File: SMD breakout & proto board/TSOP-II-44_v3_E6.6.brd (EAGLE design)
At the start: 25.4 x 27.9 mm, 7 parts

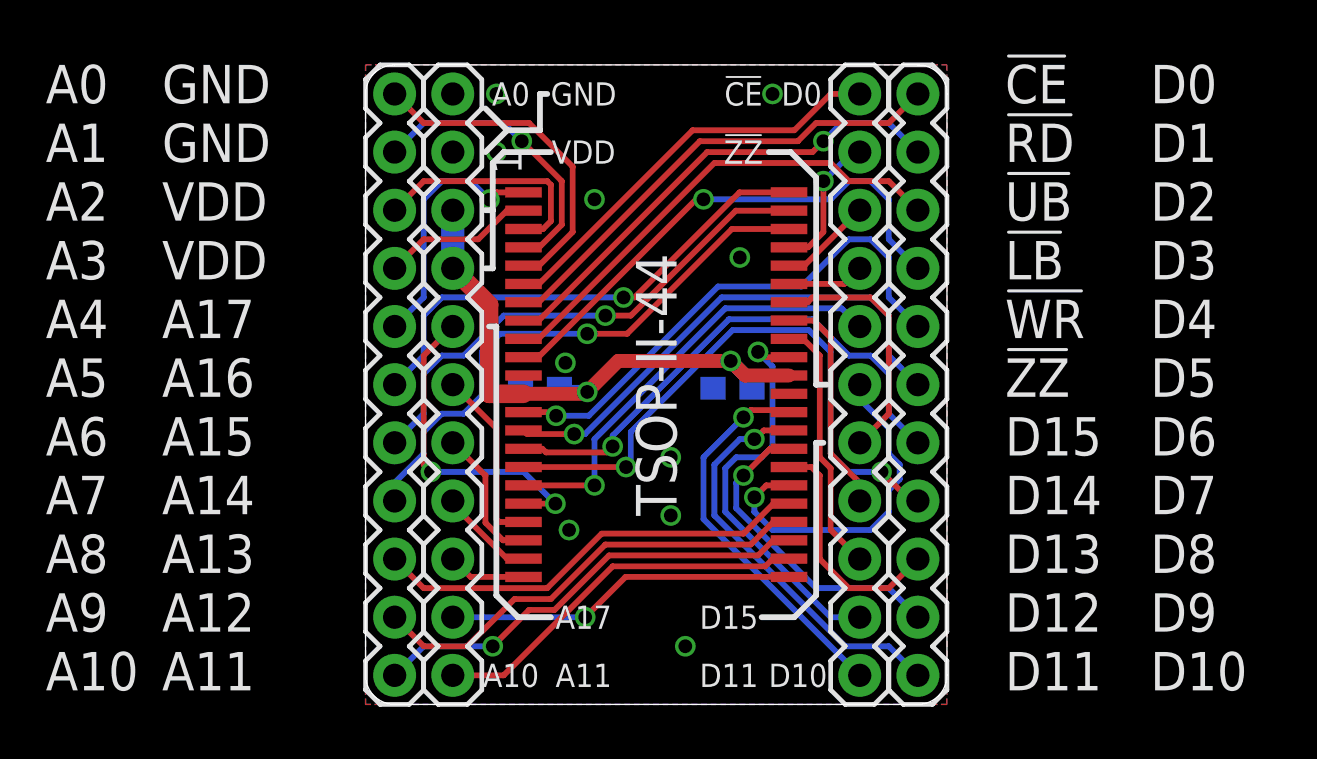
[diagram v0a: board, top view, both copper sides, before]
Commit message: swapped supply pins
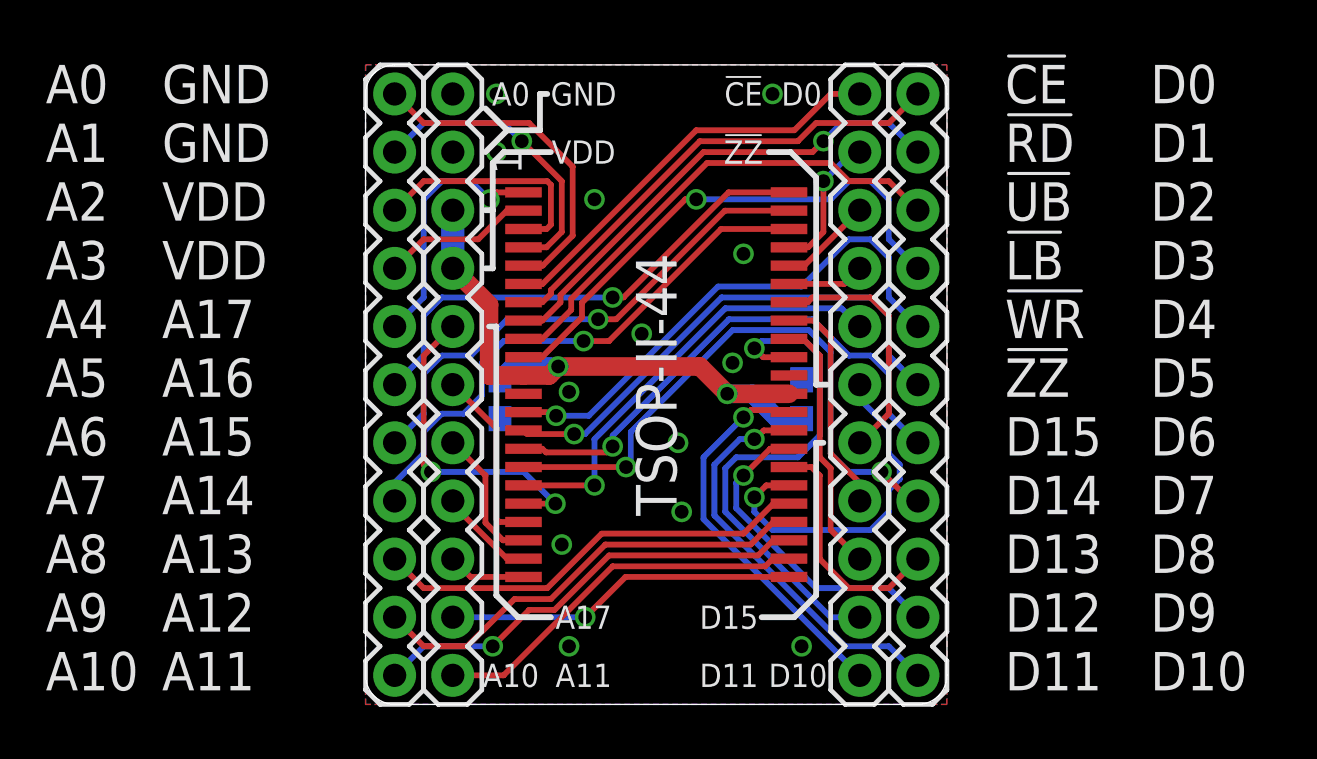
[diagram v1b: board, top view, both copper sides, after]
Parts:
- moved C2 3.05 mm to (19.1, 13.3), turned to 90 degrees
- moved C1 1.81 mm to (5.87, 13.3), turned to 270 degrees
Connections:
- net GND: now also TSOP-II-44.12, TSOP-II-44.34; no longer TSOP-II-44.11, TSOP-II-44.33
- net VDD: now also TSOP-II-44.11, TSOP-II-44.33; no longer TSOP-II-44.12, TSOP-II-44.34
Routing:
- net D12: track 18.0 -> 22.8 mm
- net VDD: track 25.5 -> 28.1 mm
